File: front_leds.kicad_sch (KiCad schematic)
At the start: 526 parts

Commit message: Major layout and placement complete
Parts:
- C1, C10, C100, C101, C102, C103, C104, C105, C106, C107, C108, C109, C11, C110, C111, C112, C113, C114, C115, C116, C117, C118, C119, C12, C120, C121, C122, C123, C124, C125, C126, C127, C128, C129, C13, C130, C131, C132, C133, C134, C135, C136, C137, C138, C139, C14, C140, C141, C142, C143, C144, C145, C146, C147, C148, C149, C15, C150, C151, C152, C153, C154, C155, C156, C157, C158, C159, C16, C160, C161, C162, C163, C164, C165, C166, C167, C168, C169, C17, C170, C171, C172, C173, C174, C175, C176, C177, C178, C179, C18, C180, C181, C182, C183, C184, C185, C186, C187, C188, C189, C19, C2, C20, C21, C22, C23, C24, C25, C26, C27, C28, C29, C3, C30, C31, C32, C33, C34, C35, C36, C37, C38, C39, C4, C40, C41, C42, C43, C44, C45, C46, C47, C48, C49, C5, C50, C51, C52, C53, C54, C55, C56, C57, C58, C59, C6, C60, C61, C62, C63, C64, C65, C66, C67, C68, C69, C7, C70, C71, C72, C73, C74, C75, C76, C77, C78, C79, C8, C80, C81, C82, C83, C84, C85, C86, C87, C88, C89, C9, C90, C91, C92, C93, C94, C95, C96, C97, C98, C99: value (none) -> 100nF; footprint (none) -> Capacitor_SMD:C_0201_0603Metric
- D1, D10, D100, D101, D102, D103, D104, D105, D106, D107, D108, D109, D11, D110, D111, D112, D113, D114, D115, D116, D117, D118, D119, D12, D120, D121, D122, D123, D124, D125, D126, D127, D128, D129, D13, D130, D131, D132, D133, D134, D135, D136, D137, D138, D139, D14, D140, D141, D142, D143, D144, D145, D146, D147, D148, D149, D15, D150, D151, D152, D153, D154, D155, D156, D157, D158, D159, D16, D160, D161, D162, D163, D164, D165, D166, D167, D168, D169, D17, D170, D171, D172, D173, D174, D175, D176, D177, D178, D179, D18, D180, D181, D182, D183, D184, D185, D186, D187, D188, D189, D19, D2, D20, D21, D22, D23, D24, D25, D26, D27, D28, D29, D3, D30, D31, D32, D33, D34, D35, D36, D37, D38, D39, D4, D40, D41, D42, D43, D44, D45, D46, D47, D48, D49, D5, D50, D51, D52, D53, D54, D55, D56, D57, D58, D59, D6, D60, D61, D62, D63, D64, D65, D66, D67, D68, D69, D7, D70, D71, D72, D73, D74, D75, D76, D77, D78, D79, D8, D80, D81, D82, D83, D84, D85, D86, D87, D88, D89, D9, D90, D91, D92, D93, D94, D95, D96, D97, D98, D99: value (none) -> WS2812B; footprint (none) -> LED_SMD:LED_WS2812B_PLCC4_5.0x5.0mm_P3.2mm
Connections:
- no-connect marks 0 -> 1

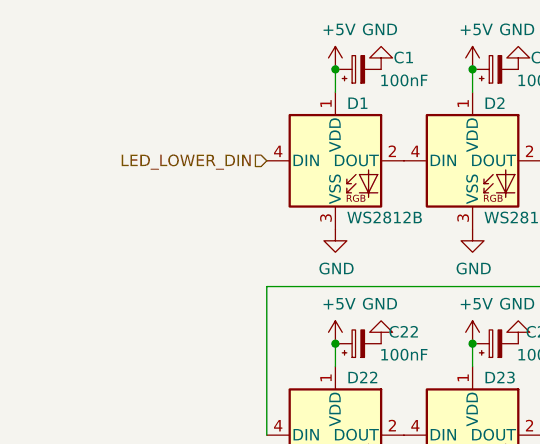
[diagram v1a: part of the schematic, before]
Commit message: DRC fixes, cap footprint update, etc.
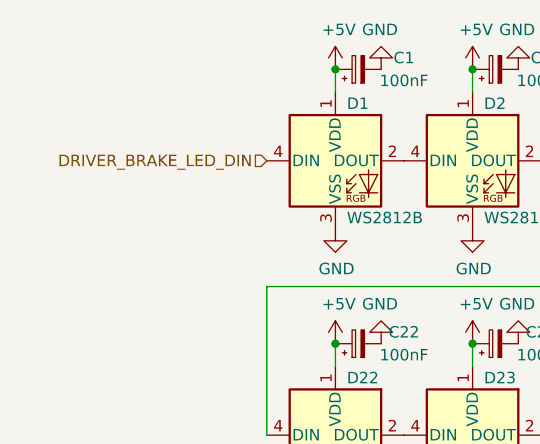
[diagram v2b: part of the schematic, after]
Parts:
- C1, C10, C100, C101, C102, C103, C104, C105, C106, C107, C108, C109, C11, C110, C111, C112, C113, C114, C115, C116, C117, C118, C119, C12, C120, C121, C122, C123, C124, C125, C126, C127, C128, C129, C13, C130, C131, C132, C133, C134, C135, C136, C137, C138, C139, C14, C140, C141, C142, C143, C144, C145, C146, C147, C148, C149, C15, C150, C151, C152, C153, C154, C155, C156, C157, C158, C159, C16, C160, C161, C162, C163, C164, C165, C166, C167, C168, C169, C17, C170, C171, C172, C173, C174, C175, C176, C177, C178, C179, C18, C180, C181, C182, C183, C184, C185, C186, C187, C188, C189, C19, C190, C191, C192, C193, C194, C195, C196, C197, C198, C199, C2, C20, C200, C201, C202, C203, C204, C205, C206, C207, C208, C209, C21, C210, C211, C212, C213, C214, C215, C216, C217, C218, C219, C22, C220, C221, C222, C223, C224, C225, C226, C227, C228, C229, C23, C230, C231, C232, C233, C234, C235, C236, C237, C238, C239, C24, C240, C241, C242, C243, C244, C245, C246, C247, C248, C249, C25, C250, C251, C252, C253, C254, C255, C256, C257, C258, C259, C26, C260, C261, C262, C263, C27, C28, C29, C3, C30, C31, C32, C33, C34, C35, C36, C37, C38, C39, C4, C40, C41, C42, C43, C44, C45, C46, C47, C48, C49, C5, C50, C51, C52, C53, C54, C55, C56, C57, C58, C59, C6, C60, C61, C62, C63, C64, C65, C66, C67, C68, C69, C7, C70, C71, C72, C73, C74, C75, C76, C77, C78, C79, C8, C80, C81, C82, C83, C84, C85, C86, C87, C88, C89, C9, C90, C91, C92, C93, C94, C95, C96, C97, C98, C99: footprint Capacitor_SMD:C_0201_0603Metric -> Capacitor_SMD:C_0402_1005Metric; LCSC (none) -> C60474
- D1, D10, D100, D101, D102, D103, D104, D105, D106, D107, D108, D109, D11, D110, D111, D112, D113, D114, D115, D116, D117, D118, D119, D12, D120, D121, D122, D123, D124, D125, D126, D127, D128, D129, D13, D130, D131, D132, D133, D134, D135, D136, D137, D138, D139, D14, D140, D141, D142, D143, D144, D145, D146, D147, D148, D149, D15, D150, D151, D152, D153, D154, D155, D156, D157, D158, D159, D16, D160, D161, D162, D163, D164, D165, D166, D167, D168, D169, D17, D170, D171, D172, D173, D174, D175, D176, D177, D178, D179, D18, D180, D181, D182, D183, D184, D185, D186, D187, D188, D189, D19, D190, D191, D192, D193, D194, D195, D196, D197, D198, D199, D2, D20, D200, D201, D202, D203, D204, D205, D206, D207, D208, D209, D21, D210, D211, D212, D213, D214, D215, D216, D217, D218, D219, D22, D220, D221, D222, D223, D224, D225, D226, D227, D228, D229, D23, D230, D231, D232, D233, D234, D235, D236, D237, D238, D239, D24, D240, D241, D242, D243, D244, D245, D246, D247, D248, D249, D25, D250, D251, D252, D253, D254, D255, D256, D257, D258, D259, D26, D260, D261, D262, D263, D27, D28, D29, D3, D30, D31, D32, D33, D34, D35, D36, D37, D38, D39, D4, D40, D41, D42, D43, D44, D45, D46, D47, D48, D49, D5, D50, D51, D52, D53, D54, D55, D56, D57, D58, D59, D6, D60, D61, D62, D63, D64, D65, D66, D67, D68, D69, D7, D70, D71, D72, D73, D74, D75, D76, D77, D78, D79, D8, D80, D81, D82, D83, D84, D85, D86, D87, D88, D89, D9, D90, D91, D92, D93, D94, D95, D96, D97, D98, D99: LCSC (none) -> C114586
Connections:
- net LED_LOWER_DIN renamed DRIVER_BRAKE_LED_DIN
